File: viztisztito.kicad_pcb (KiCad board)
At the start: 2 copper layers, 180 x 108 mm, 153 parts, among them J1 +5V, J2 +3.3V, J3 GND, J4 CURR_DIRECT, J5 CURR_FILT, J6 Micro_SD_Card_Det, J7 USB_OTG, Q1 BS250, Q2 BC850, SW1 SW_PUSH, SW2 SW_PUSH, U1 VTX-214-020-115, U10 MAX803, U2 RT7297BHZSP, U3 RT7297BHZSP, U4 TLP293-4, U5 ACS722, U6 MCP3004, U7 TC77, U8 SN74AHC1G125DBVR, U9 FT230XQ

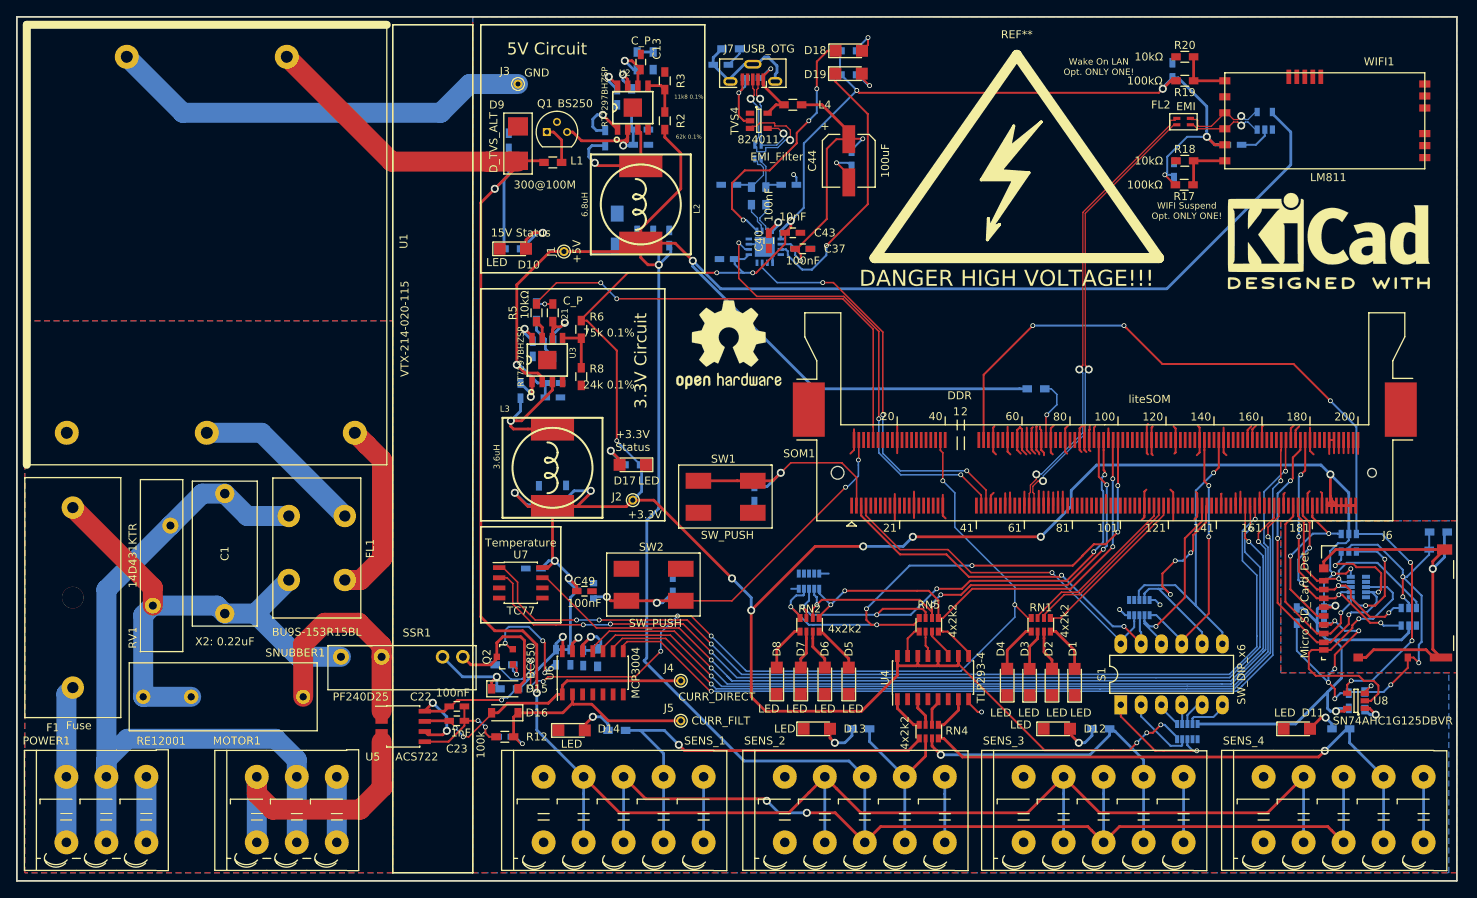
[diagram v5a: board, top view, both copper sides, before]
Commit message: mounting holes and final touches
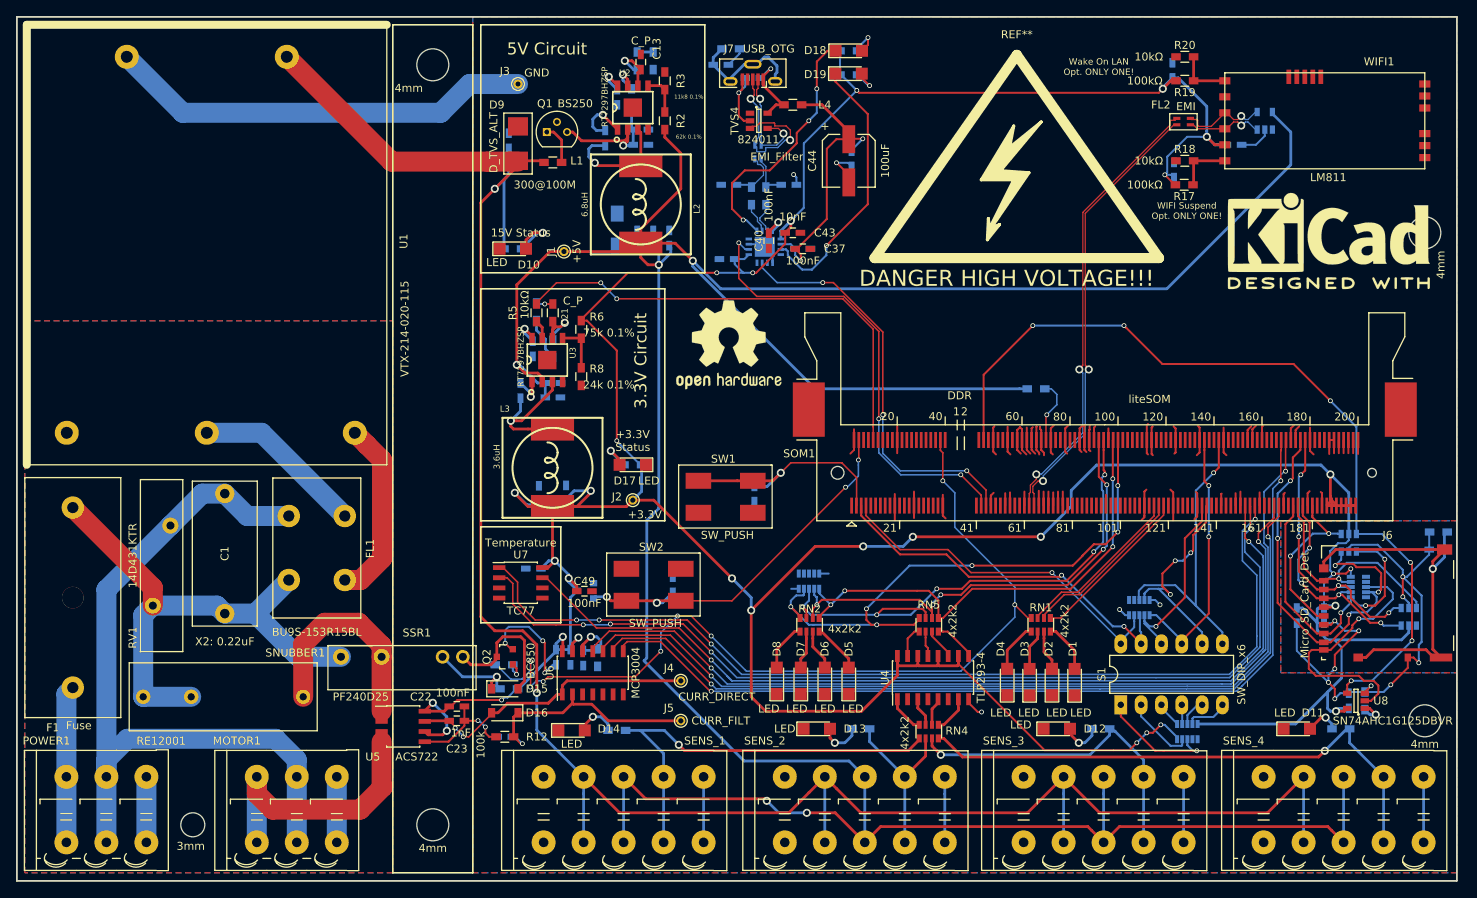
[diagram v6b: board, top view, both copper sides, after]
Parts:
- added 3mm: Mounting Hole 3mm, water:Mounting_Hole_3mm, F.Cu at (43.0, 138.0)
- added 4mm: Mounting Hole 4mm, water:Mounting_Hole_4mm, F.Cu at (73.0, 43.0)
- added 4mm: Mounting Hole 4mm, water:Mounting_Hole_4mm, F.Cu at (73.0, 138.0)
- added 4mm: Mounting Hole 4mm, water:Mounting_Hole_4mm, F.Cu at (197.0, 64.0)
- added 4mm: Mounting Hole 4mm, water:Mounting_Hole_4mm, F.Cu at (197.0, 125.0)
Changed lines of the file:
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@@
     (tracks 1934)
     (zones 0)
-    (modules 153)
+    (modules 158)
     (nets 246)
   )
@@
     (add_net "Net-(R14-Pad2)")
   )
+  (module water:Mounting_Hole_3mm (layer F.Cu)
+    (at 43 138)
+    (fp_text reference 3mm (at -0.254 2.667) (layer F.SilkS)
+      (effects (font (size 1 1) (thickness 0.15)))
+    )
+    (fp_text value "Mounting Hole 3mm" (at 0.127 -2.286) (layer F.Fab) hide
+      (effects (font (size 1 1) (thickness 0.15)))
+    )
+    (pad "" np_thru_hole circle (at 0 0) (size 3 3) (drill 3) (layers *.Cu *.Mask))
+  )
+  (module water:Mounting_Hole_4mm (layer F.Cu)
+    (at 73 43)
+    (fp_text reference 4mm (at -3 2.921) (layer F.SilkS)
+      (effects (font (size 1 1) (thickness 0.15)))
+    )
+    (fp_text value "Mounting Hole 4mm" (at 0.127 -3.175) (layer F.Fab) hide
+      (effects (font (size 1 1) (thickness 0.15)))
+    )
+    (pad "" np_thru_hole circle (at 0 0) (size 4 4) (drill 4) (layers *.Cu *.Mask))
+  )
+  (module water:Mounting_Hole_4mm (layer F.Cu)
+    (at 73 138)
+    (fp_text reference 4mm (at 0 2.921) (layer F.SilkS)
+      (effects (font (size 1 1) (thickness 0.15)))
+    )
+    (fp_text value "Mounting Hole 4mm" (at 0.127 -3.175) (layer F.Fab) hide
+      (effects (font (size 1 1) (thickness 0.15)))
+    )
+    (pad "" np_thru_hole circle (at 0 0) (size 4 4) (drill 4) (layers *.Cu *.Mask))
+  )
+  (module water:Mounting_Hole_4mm (layer F.Cu)
+    (at 197 64)
+    (fp_text reference 4mm (at 2 4 90) (layer F.SilkS)
+      (effects (font (size 1 1) (thickness 0.15)))
+    )
+    (fp_text value "Mounting Hole 4mm" (at 0.127 -3.175) (layer F.Fab) hide
+      (effects (font (size 1 1) (thickness 0.15)))
+    )
+    (pad "" np_thru_hole circle (at 0 0) (size 4 4) (drill 4) (layers *.Cu *.Mask))
+  )
+  (module water:Mounting_Hole_4mm (layer F.Cu)
+    (at 197 125)
+    (fp_text reference 4mm (at 0 2.921) (layer F.SilkS)
+      (effects (font (size 1 1) (thickness 0.15)))
+    )
+    (fp_text value "Mounting Hole 4mm" (at 0.127 -3.175) (layer F.Fab) hide
+      (effects (font (size 1 1) (thickness 0.15)))
+    )
+    (pad "" np_thru_hole circle (at 0 0) (size 4 4) (drill 4) (layers *.Cu *.Mask))
+  )
   (module Capacitors_THT:C_Rect_L18.0mm_W8.0mm_P15.00mm_FKS3_FKP3 (layer F.Cu)
     (at 47 111.6 90)
@@
       (effects (font (size 1 1) (thickness 0.15)))
     )
-    (fp_text value CONN_01X03 (at 16.3 2 90) (layer F.Fab)
+    (fp_text value CONN_01X03 (at 16.3 2 90) (layer F.Fab) hide
       (effects (font (size 1 1) (thickness 0.15)))
     )
@@
     (polygon
       (pts
-        (xy 78 37) (xy 78 144) (xy 200 144) (xy 200 119) (xy 179 119)
+        (xy 78 37) (xy 78 144) (xy 201 144) (xy 201 119) (xy 179 119)
         (xy 179 100) (xy 201 100) (xy 201 37)
       )

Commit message: BOM version
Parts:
- moved 4mm 1.00 mm to (197.0, 124.0)
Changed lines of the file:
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@@
   )
   (module water:Mounting_Hole_4mm (layer F.Cu)
-    (at 197 125)
+    (at 197 124)
     (fp_text reference 4mm (at 0 2.921) (layer F.SilkS)
       (effects (font (size 1 1) (thickness 0.15)))

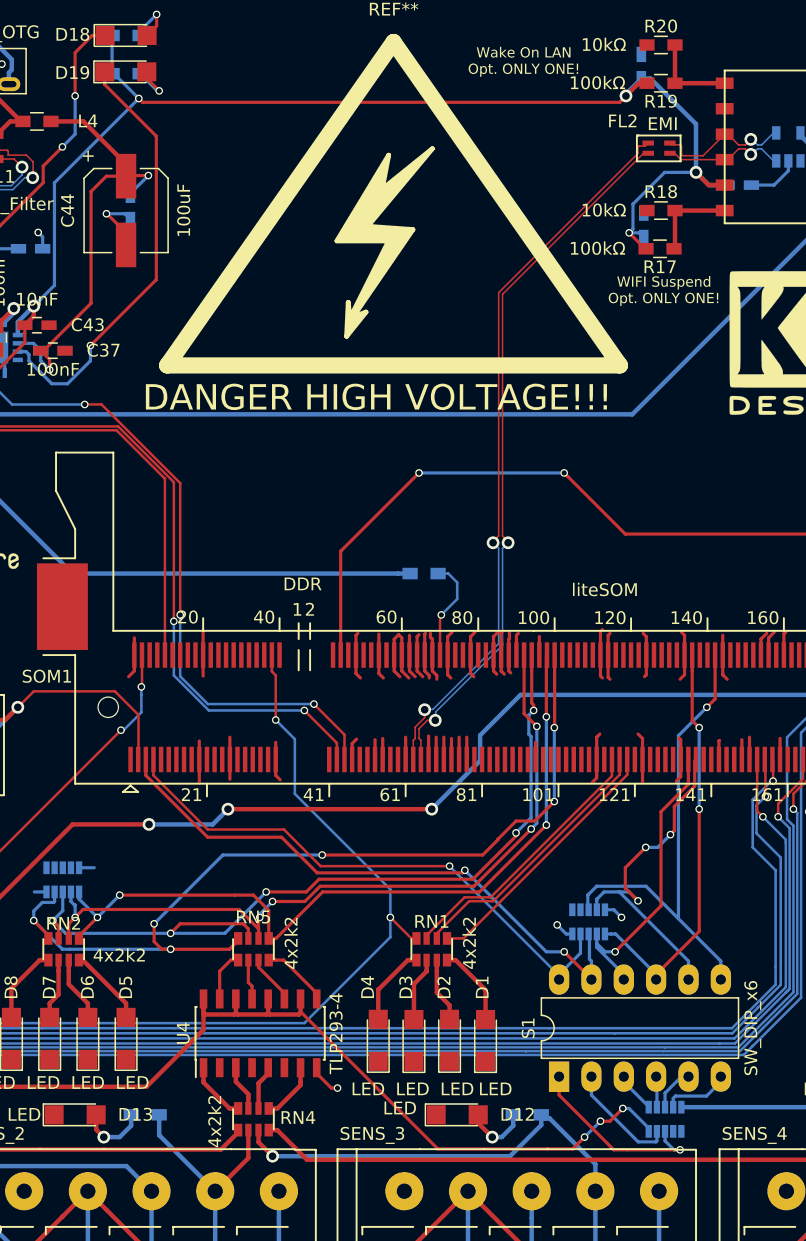
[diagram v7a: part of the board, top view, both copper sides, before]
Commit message: This version contains the final revision before the part footprint verification.
- The fuse is now moved outside of the power module before any parts
- The wifi module has an additional pair of 22R differential resistors
- The minor moves in the power power supply of the wifi module
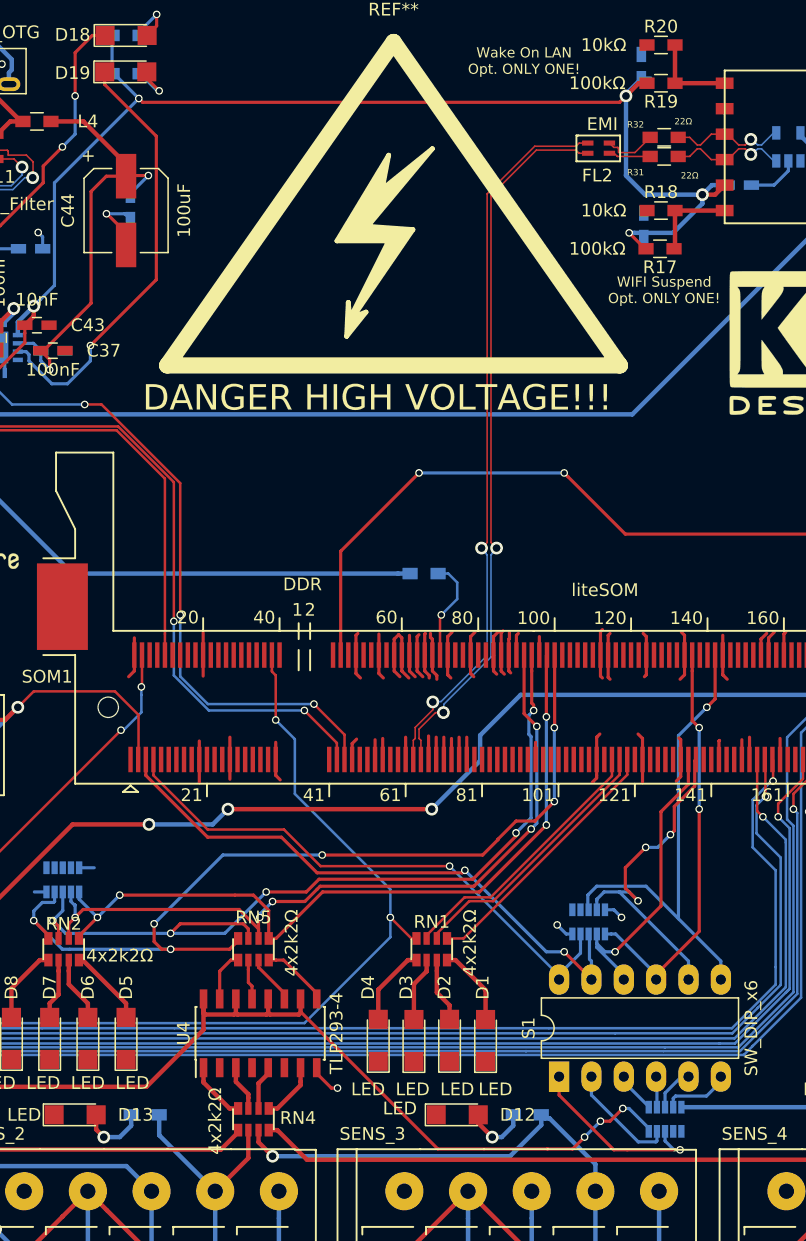
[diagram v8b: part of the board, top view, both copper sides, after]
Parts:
- added R31: 22Ω, Resistors_SMD:R_0603_HandSoldering, F.Cu at (167.2, 50.8)
- added R32: 22Ω, Resistors_SMD:R_0603_HandSoldering, F.Cu at (167.2, 49.2)
- R11: value 150 -> 150Ω
- R22, R23: value 22 -> 22Ω
- R4: value 33k -> 33kΩ
- R9: value 22k -> 22kΩ
- RN1, RN2, RN4, RN5: value 4x2k2 -> 4x2k2Ω
- RN6: value 4x47k -> 4x47kΩ
- moved FL2 4.75 mm to (161.2, 50.5)
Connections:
- net 230V_AC+ renamed Net-(F1-Pad2)
- FL2 pad 2: /system_on_module/wifi/F_USB1_D_N -> /system_on_module/wifi/F_USB1_DIFF_N
- FL2 pad 3: /system_on_module/wifi/F_USB1_D_P -> /system_on_module/wifi/F_USB1_DIFF_P
- R5 pad 2: /PMIC_ON_REQ -> /PWR_module/PMIC_ON_REQ
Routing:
- net /PWR_module/PMIC_ON_REQ: track 0.00 -> 59.5 mm, vias 0 -> 2
- net /PMIC_ON_REQ: track 59.5 -> 0.00 mm, vias 2 -> 0
- net /system_on_module/wifi/F_USB1_DIFF_P: track 0.00 -> 4.19 mm
- net /system_on_module/wifi/F_USB1_DIFF_N: track 0.00 -> 3.30 mm
- net +3.3V: track 527.0 -> 528.9 mm
- net /system_on_module/wifi/F_USB1_D_P: track 11.0 -> 9.40 mm
- net /system_on_module/USB_OTG1_D_N: track 56.1 -> 56.6 mm
